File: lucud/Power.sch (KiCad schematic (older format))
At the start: 1 part, among them U2 R-78E3.3-0.5

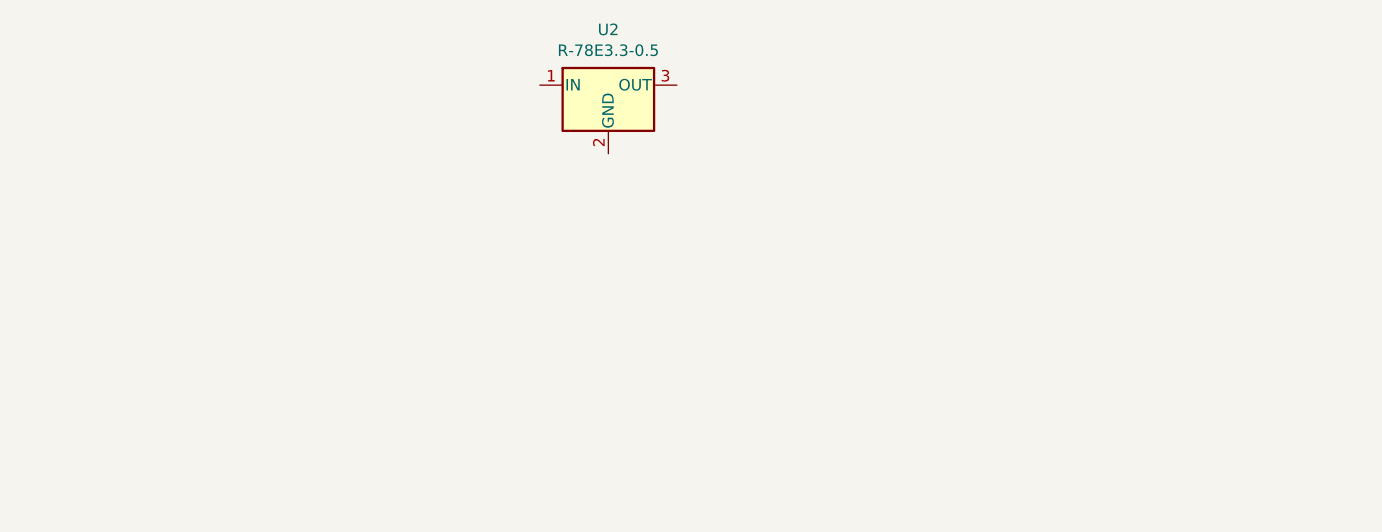
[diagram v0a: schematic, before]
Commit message: Added power headers and some caps for the pcb.
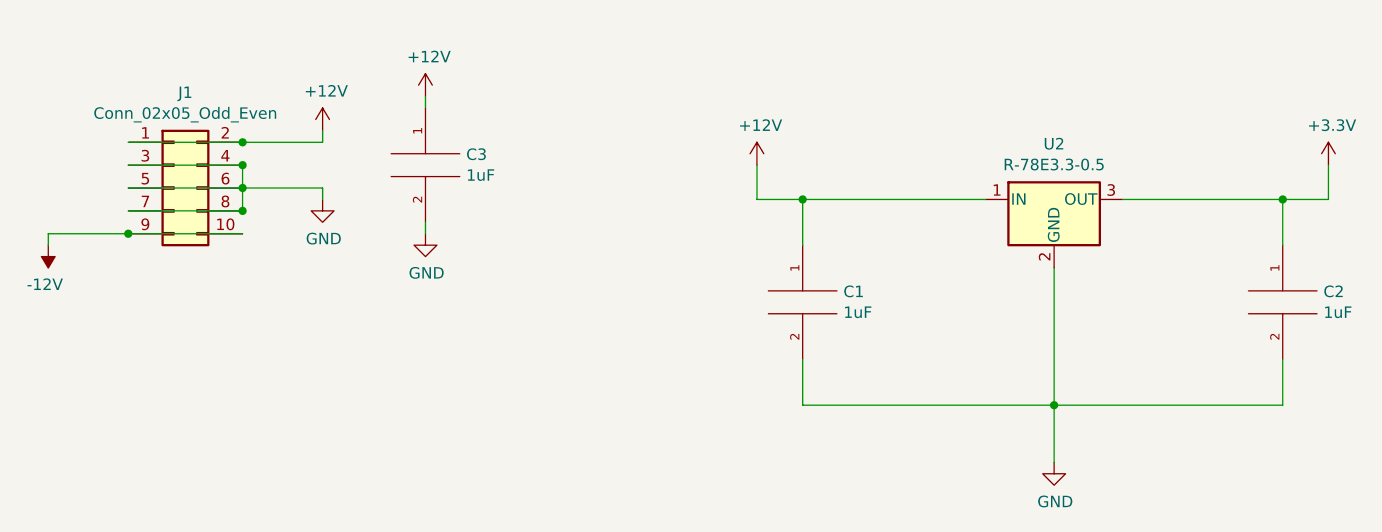
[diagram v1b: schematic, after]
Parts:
- added C1, C2, C3: 1uF, Capacitor_SMD:C_0603_1608Metric, symbol pspice:CAP
- added J1: Conn_02x05_Odd_Even, Connector_PinHeader_2.54mm:PinHeader_2x05_P2.54mm_Vertical, symbol Connector_Generic:Conn_02x05_Odd_Even
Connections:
- net +12V: now reaches U2.1 (IN)
- net +12V: now also C1.1, C3.1, J1.1 (Pin_1), J1.2 (Pin_2)
- net GND: now reaches U2.2 (GND)
- net GND: now also C1.2, C2.2, C3.2, J1.3 (Pin_3), J1.4 (Pin_4), J1.5 (Pin_5), J1.6 (Pin_6), J1.7 (Pin_7), J1.8 (Pin_8)
- net +3V3: now reaches U2.3 (OUT)
- net +3V3: now also C2.1
- new net -12V: J1.10 (Pin_10), J1.9 (Pin_9)
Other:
- moved on the sheet: U2
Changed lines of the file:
@@
 L Regulator_Switching:R-78E3.3-0.5 U2
 U 1 1 5C243CB2
-P 3900 3100
-F 0 "U2" H 3900 3342 50  0000 C CNN
-F 1 "R-78E3.3-0.5" H 3900 3251 50  0000 C CNN
-F 2 "Converter_DCDC:Converter_DCDC_RECOM_R-78E-0.5_THT" H 3950 2850 50  0001 L CIN
-F 3 "https://www.recom-power.com/pdf/Innoline/R-78Exx-0.5.pdf" H 3900 3100 50  0001 C CNN
-	1    3900 3100
-	1    0    0    -1
-$EndComp
+P 5850 3600
+F 0 "U2" H 5850 3842 50  0000 C CNN
+F 1 "R-78E3.3-0.5" H 5850 3751 50  0000 C CNN
+F 2 "Converter_DCDC:Converter_DCDC_RECOM_R-78E-0.5_THT" H 5900 3350 50  0001 L CIN
+F 3 "https://www.recom-power.com/pdf/Innoline/R-78Exx-0.5.pdf" H 5850 3600 50  0001 C CNN
+	1    5850 3600
+	1    0    0    -1
+$EndComp
+$Comp
+L pspice:CAP C2
+U 1 1 5C2441A0
+P 6850 4050
+F 0 "C2" H 7028 4096 50  0000 L CNN
+F 1 "1uF" H 7028 4005 50  0000 L CNN
+F 2 "Capacitor_SMD:C_0603_1608Metric" H 6850 4050 50  0001 C CNN
+F 3 "~" H 6850 4050 50  0001 C CNN
+	1    6850 4050
+	1    0    0    -1
+$EndComp
+$Comp
+L pspice:CAP C1
+U 1 1 5C2441F8
+P 4750 4050
+F 0 "C1" H 4928 4096 50  0000 L CNN
+F 1 "1uF" H 4928 4005 50  0000 L CNN
+F 2 "Capacitor_SMD:C_0603_1608Metric" H 4750 4050 50  0001 C CNN
+F 3 "~" H 4750 4050 50  0001 C CNN
+	1    4750 4050
+	1    0    0    -1
+$EndComp
+Wire Wire Line
+	5550 3600 4750 3600
+Wire Wire Line
+	4750 3800 4750 3600
+Connection ~ 4750 3600
+Wire Wire Line
+	4750 3600 4550 3600
+Wire Wire Line
+	6150 3600 6850 3600
+Wire Wire Line
+	6850 3800 6850 3600
+Connection ~ 6850 3600
+Wire Wire Line
+	6850 3600 7050 3600
+Wire Wire Line
+	5850 3900 5850 4500
+Wire Wire Line
+	4750 4300 4750 4500
+Wire Wire Line
+	4750 4500 5850 4500
+Connection ~ 5850 4500
+Wire Wire Line
+	6850 4300 6850 4500
+Wire Wire Line
+	6850 4500 5850 4500
+$Comp
+L power:GND #PWR01
+U 1 1 5C2443CA
+P 5850 4750
+F 0 "#PWR01" H 5850 4500 50  0001 C CNN
+F 1 "GND" H 5855 4577 50  0000 C CNN
+F 2 "" H 5850 4750 50  0001 C CNN
+F 3 "" H 5850 4750 50  0001 C CNN
+	1    5850 4750
+	1    0    0    -1
+$EndComp
+Wire Wire Line
+	5850 4500 5850 4750
+$Comp
+L power:+12V #PWR07
+U 1 1 5C244519
+P 4550 3450
+F 0 "#PWR07" H 4550 3300 50  0001 C CNN
+F 1 "+12V" H 4565 3623 50  0000 C CNN
+F 2 "" H 4550 3450 50  0001 C CNN
+F 3 "" H 4550 3450 50  0001 C CNN
+	1    4550 3450
+	1    0    0    -1
+$EndComp
+Wire Wire Line
+	4550 3450 4550 3600
+$Comp
+L power:+3.3V #PWR08
+U 1 1 5C2448FE
+P 7050 3450
+F 0 "#PWR08" H 7050 3300 50  0001 C CNN
+F 1 "+3.3V" H 7065 3623 50  0000 C CNN
+F 2 "" H 7050 3450 50  0001 C CNN
+F 3 "" H 7050 3450 50  0001 C CNN
+	1    7050 3450
+	1    0    0    -1
+$EndComp
+Wire Wire Line
+	7050 3450 7050 3600
+$Comp
+L Connector_Generic:Conn_02x05_Odd_Even J1
+U 1 1 5C2453E2
+P 2000 3550
+F 0 "J1" H 2050 3967 50  0000 C CNN
+F 1 "Conn_02x05_Odd_Even" H 2050 3876 50  0000 C CNN
+F 2 "Connector_PinHeader_2.54mm:PinHeader_2x05_P2.54mm_Vertical" H 2000 3550 50  0001 C CNN
+F 3 "~" H 2000 3550 50  0001 C CNN
+	1    2000 3550
+	1    0    0    -1
+$EndComp
+Wire Wire Line
+	1800 3450 2300 3450
+Wire Wire Line
+	1800 3550 2300 3550
+Wire Wire Line
+	1800 3650 2300 3650
+Wire Wire Line
+	2300 3450 2300 3550
+Connection ~ 2300 3450
+Connection ~ 2300 3650
+Connection ~ 2300 3550
+Wire Wire Line
+	2300 3550 2300 3650
+Wire Wire Line
+	2300 3550 2650 3550
+Wire Wire Line
+	2650 3550 2650 3600
+$Comp
+L power:+12V #PWR03
+U 1 1 5C245C30
+P 2650 3300
+F 0 "#PWR03" H 2650 3150 50  0001 C CNN
+F 1 "+12V" H 2665 3473 50  0000 C CNN
+F 2 "" H 2650 3300 50  0001 C CNN
+F 3 "" H 2650 3300 50  0001 C CNN
+	1    2650 3300
+	1    0    0    -1
+$EndComp
+$Comp
+L power:GND #PWR04
+U 1 1 5C245C63
+P 2650 3600
+F 0 "#PWR04" H 2650 3350 50  0001 C CNN
+F 1 "GND" H 2655 3427 50  0000 C CNN
+F 2 "" H 2650 3600 50  0001 C CNN
+F 3 "" H 2650 3600 50  0001 C CNN
+	1    2650 3600
+	1    0    0    -1
+$EndComp
+Wire Wire Line
+	1800 3350 2300 3350
+Wire Wire Line
+	2300 3350 2650 3350
+Wire Wire Line
+	2650 3350 2650 3300
+Connection ~ 2300 3350
+Wire Wire Line
+	2300 3750 1800 3750
+Wire Wire Line
+	1800 3750 1450 3750
+Wire Wire Line
+	1450 3750 1450 3800
+Connection ~ 1800 3750
+$Comp
+L power:-12V #PWR02
+U 1 1 5C246C92
+P 1450 3800
+F 0 "#PWR02" H 1450 3900 50  0001 C CNN
+F 1 "-12V" H 1465 3973 50  0000 C CNN
+F 2 "" H 1450 3800 50  0001 C CNN
+F 3 "" H 1450 3800 50  0001 C CNN
+	1    1450 3800
+	-1   0    0    1
+$EndComp
+$Comp
+L pspice:CAP C3
+U 1 1 5C246EA0
+P 3100 3450
+F 0 "C3" H 3278 3496 50  0000 L CNN
+F 1 "1uF" H 3278 3405 50  0000 L CNN
+F 2 "Capacitor_SMD:C_0603_1608Metric" H 3100 3450 50  0001 C CNN
+F 3 "~" H 3100 3450 50  0001 C CNN
+	1    3100 3450
+	1    0    0    -1
+$EndComp
+$Comp
+L power:+12V #PWR05
+U 1 1 5C246F19
+P 3100 3150
+F 0 "#PWR05" H 3100 3000 50  0001 C CNN
+F 1 "+12V" H 3115 3323 50  0000 C CNN
+F 2 "" H 3100 3150 50  0001 C CNN
+F 3 "" H 3100 3150 50  0001 C CNN
+	1    3100 3150
+	1    0    0    -1
+$EndComp
+$Comp
+L power:GND #PWR06
+U 1 1 5C246F1F
+P 3100 3750
+F 0 "#PWR06" H 3100 3500 50  0001 C CNN
+F 1 "GND" H 3105 3577 50  0000 C CNN
+F 2 "" H 3100 3750 50  0001 C CNN
+F 3 "" H 3100 3750 50  0001 C CNN
+	1    3100 3750
+	1    0    0    -1
+$EndComp
+Wire Wire Line
+	3100 3750 3100 3700
+Wire Wire Line
+	3100 3200 3100 3150
 $EndSCHEMATC
